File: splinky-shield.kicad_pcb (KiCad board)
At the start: 2 copper layers, 73.5 x 50.8 mm, 55 parts, among them J1 USB_C_Receptacle_USB2.0, J10 Ribbon, J2 Conn_01x04_Female, J3 Conn_01x04_Female, J5 Conn_01x02, J50 Conn_01x04_Female, J6 Serial, J7 trackball, J8 Ribbon, J9 RGB, SW1 SW_Push, SW2 SW_Push, SW3 SW_SPST, U1 RP2040, U2 GD25Q80CEIGR, U3 XC6210B332MR-G, Y1 Crystal_GND24

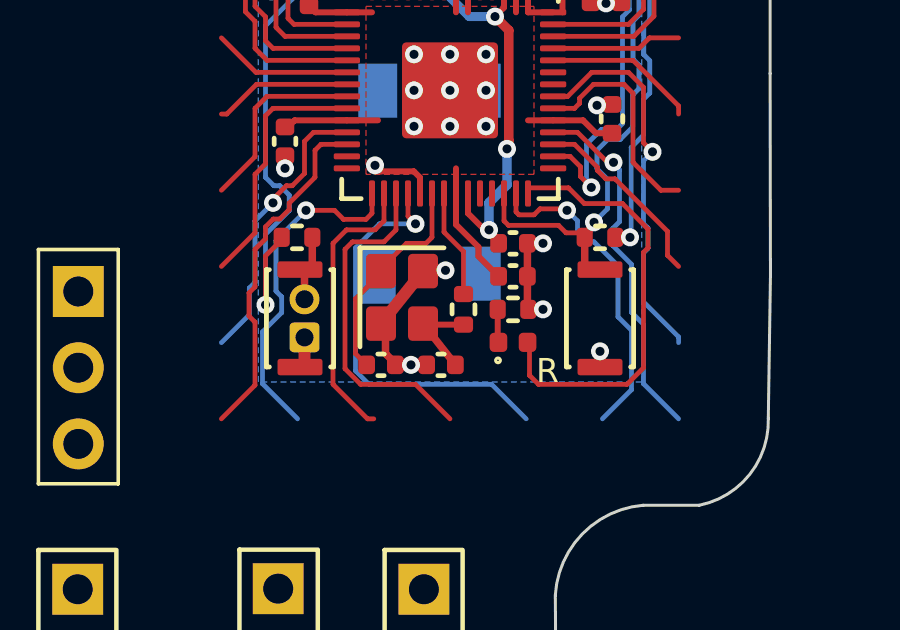
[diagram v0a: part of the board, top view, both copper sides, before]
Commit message: remove buttons
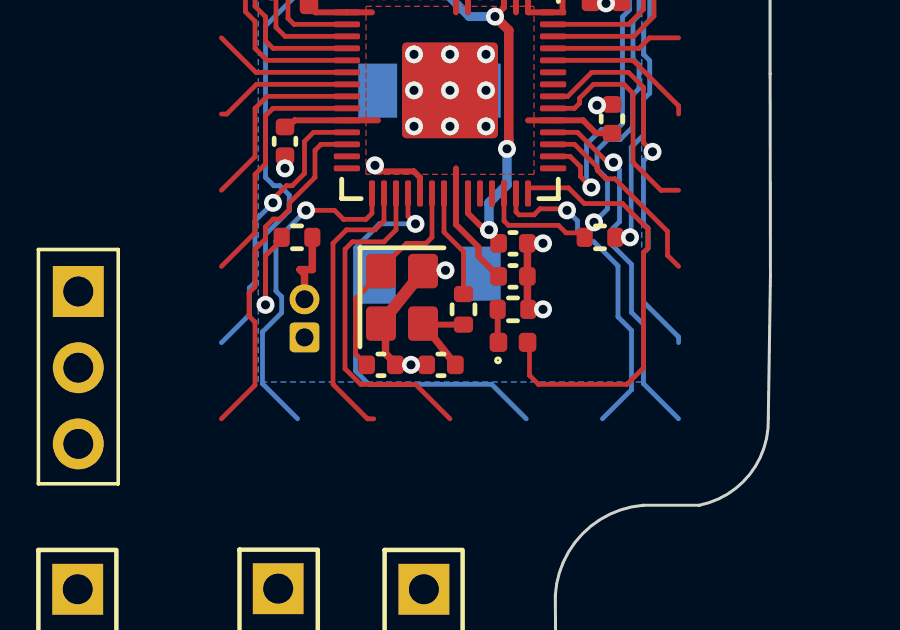
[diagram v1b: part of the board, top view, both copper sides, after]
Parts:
- removed SW1, SW2: SW_Push, Button_Switch_SMD:SW_SPST_CK_KXT3
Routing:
- net GND: track 24.8 -> 23.2 mm, vias 24 -> 23
- net Rst: track 22.0 -> 20.4 mm
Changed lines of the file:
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@@
     )
   )
-  (footprint "Button_Switch_SMD:SW_SPST_CK_KXT3" (layer "F.Cu")
-    (at 147.4 104.6 90)
-    (descr "https://www.ckswitches.com/media/1465/kxt3.pdf")
-    (tags "Switch SPST KXT3")
-    (property "LCSC" "C319433")
-    (property "Sheetfile" "splinky-shield.kicad_sch")
-    (property "Sheetname" "")
-    (attr smd)
-    (fp_text reference "SW2" (at 0 -2 90) (layer "F.SilkS") hide
-      (effects (font (size 1 1) (thickness 0.15)))
-    )
-    (fp_text value "SW_Push" (at 0 2 90) (layer "F.Fab")
-      (effects (font (size 1 1) (thickness 0.15)))
-    )
-    (fp_text user "${REFERENCE}" (at 0 0 90) (layer "F.Fab") hide
-      (effects (font (size 0.5 0.5) (thickness 0.075)))
-    )
-    (fp_line (start 1.62 -1.12) (end 1.62 -1.02) (layer "F.SilkS") (width 0.16))
-    (fp_line (start 1.62 1.02) (end 1.62 1.12) (layer "F.SilkS") (width 0.16))
-    (fp_line (start -1.62 1.12) (end 1.62 1.12) (layer "F.SilkS") (width 0.16))
-    (fp_line (start -1.62 1.02) (end -1.62 1.12) (layer "F.SilkS") (width 0.16))
-    (fp_line (start -1.62 -1.12) (end 1.62 -1.12) (layer "F.SilkS") (width 0.16))
-    (fp_line (start -1.62 -1.12) (end -1.62 -1.02) (layer "F.SilkS") (width 0.16))
-    (fp_line (start 2.15 -1.25) (end 2.15 1.25) (layer "F.CrtYd") (width 0.05))
-    (fp_line (start -2.15 1.25) (end 2.15 1.25) (layer "F.CrtYd") (width 0.05))
-    (fp_line (start -2.15 -1.25) (end 2.15 -1.25) (layer "F.CrtYd") (width 0.05))
-    (fp_line (start -2.15 -1.25) (end -2.15 1.25) (layer "F.CrtYd") (width 0.05))
-    (fp_line (start -1.75 0.65) (end -1.5 0.65) (layer "F.Fab") (width 0.1))
-    (fp_line (start -1.5 -1) (end 1.5 -1) (layer "F.Fab") (width 0.1))
-    (fp_line (start 1.75 0.4) (end 1.75 0.65) (layer "F.Fab") (width 0.1))
-    (fp_line (start 1.75 -0.65) (end 1.75 -0.4) (layer "F.Fab") (width 0.1))
-    (fp_line (start -1.75 -0.65) (end -1.75 -0.4) (layer "F.Fab") (width 0.1))
-    (fp_line (start -1.75 0.4) (end -1.75 0.65) (layer "F.Fab") (width 0.1))
-    (fp_line (start -1.75 -0.4) (end -1.5 -0.15) (layer "F.Fab") (width 0.1))
-    (fp_line (start 1.75 -0.4) (end 1.5 -0.15) (layer "F.Fab") (width 0.1))
-    (fp_line (start 1.5 -0.65) (end 1.75 -0.65) (layer "F.Fab") (width 0.1))
-    (fp_line (start -1.5 0.15) (end -1.75 0.4) (layer "F.Fab") (width 0.1))
-    (fp_line (start 1.5 0.15) (end 1.75 0.4) (layer "F.Fab") (width 0.1))
-    (fp_line (start -1.5 -0.65) (end -1.75 -0.65) (layer "F.Fab") (width 0.1))
-    (fp_line (start 1.75 0.65) (end 1.5 0.65) (layer "F.Fab") (width 0.1))
-    (fp_line (start 1.5 1) (end -1.5 1) (layer "F.Fab") (width 0.1))
-    (fp_line (start -1.5 1) (end -1.5 -1) (layer "F.Fab") (width 0.1))
-    (fp_line (start 1.5 -1) (end 1.5 1) (layer "F.Fab") (width 0.1))
-    (pad "1" smd roundrect (at -1.625 0 90) (size 0.55 1.5) (layers "F.Cu" "F.Paste" "F.Mask") (roundrect_rratio 0.15)
-      (net 2 "GND") (pinfunction "1") (pintype "passive"))
-    (pad "2" smd roundrect (at 1.625 0 90) (size 0.55 1.5) (layers "F.Cu" "F.Paste" "F.Mask") (roundrect_rratio 0.15)
-      (net 47 "Net-(J5-Pad2)") (pinfunction "2") (pintype "passive"))
-    (model "${KICAD6_3DMODEL_DIR}/Button_Switch_SMD.3dshapes/SW_SPST_CK_KXT3.wrl"
-      (offset (xyz 0 0 0))
-      (scale (xyz 1 1 1))
-      (rotate (xyz 0 0 0))
-    )
-    (model "${KICAD6_USER_LIB}/3D_models/SW_SPST_CnK_KXT3.step"
-      (offset (xyz 0 0 0))
-      (scale (xyz 1 1 1))
-      (rotate (xyz 0 0 0))
-    )
-  )
   (footprint "Capacitor_SMD:C_0402_1005Metric" (layer "F.Cu")
     (at 154.5 102.1)
@@
     )
   )
-  (footprint "Button_Switch_SMD:SW_SPST_CK_KXT3" (layer "F.Cu")
-    (at 157.4 104.6 90)
-    (descr "https://www.ckswitches.com/media/1465/kxt3.pdf")
-    (tags "Switch SPST KXT3")
-    (property "LCSC" "C319433")
-    (property "Sheetfile" "splinky-shield.kicad_sch")
-    (property "Sheetname" "")
-    (attr smd)
-    (fp_text reference "SW1" (at 0 -2 90) (layer "F.SilkS") hide
-      (effects (font (size 1 1) (thickness 0.15)))
-    )
-    (fp_text value "SW_Push" (at 0 2 90) (layer "F.Fab")
-      (effects (font (size 1 1) (thickness 0.15)))
-    )
-    (fp_text user "R" (at -1.75 -1.75 unlocked) (layer "F.SilkS")
-      (effects (font (size 0.8 0.8) (thickness 0.2)))
-    )
-    (fp_text user "${REFERENCE}" (at 0 0 90) (layer "F.Fab") hide
-      (effects (font (size 0.5 0.5) (thickness 0.075)))
-    )
-    (fp_line (start -1.62 1.12) (end 1.62 1.12) (layer "F.SilkS") (width 0.16))
-    (fp_line (start -1.62 -1.12) (end 1.62 -1.12) (layer "F.SilkS") (width 0.16))
-    (fp_line (start 1.62 -1.12) (end 1.62 -1.02) (layer "F.SilkS") (width 0.16))
-    (fp_line (start 1.62 1.02) (end 1.62 1.12) (layer "F.SilkS") (width 0.16))
-    (fp_line (start -1.62 1.02) (end -1.62 1.12) (layer "F.SilkS") (width 0.16))
-    (fp_line (start -1.62 -1.12) (end -1.62 -1.02) (layer "F.SilkS") (width 0.16))
-    (fp_line (start -2.15 -1.25) (end 2.15 -1.25) (layer "F.CrtYd") (width 0.05))
-    (fp_line (start 2.15 -1.25) (end 2.15 1.25) (layer "F.CrtYd") (width 0.05))
-    (fp_line (start -2.15 1.25) (end 2.15 1.25) (layer "F.CrtYd") (width 0.05))
-    (fp_line (start -2.15 -1.25) (end -2.15 1.25) (layer "F.CrtYd") (width 0.05))
-    (fp_line (start -1.75 -0.4) (end -1.5 -0.15) (layer "F.Fab") (width 0.1))
-    (fp_line (start -1.5 -1) (end 1.5 -1) (layer "F.Fab") (width 0.1))
-    (fp_line (start -1.75 0.4) (end -1.75 0.65) (layer "F.Fab") (width 0.1))
-    (fp_line (start 1.75 -0.4) (end 1.5 -0.15) (layer "F.Fab") (width 0.1))
-    (fp_line (start 1.5 -0.65) (end 1.75 -0.65) (layer "F.Fab") (width 0.1))
-    (fp_line (start 1.5 0.15) (end 1.75 0.4) (layer "F.Fab") (width 0.1))
-    (fp_line (start -1.5 -0.65) (end -1.75 -0.65) (layer "F.Fab") (width 0.1))
-    (fp_line (start 1.75 -0.65) (end 1.75 -0.4) (layer "F.Fab") (width 0.1))
-    (fp_line (start -1.5 0.15) (end -1.75 0.4) (layer "F.Fab") (width 0.1))
-    (fp_line (start -1.5 1) (end -1.5 -1) (layer "F.Fab") (width 0.1))
-    (fp_line (start 1.75 0.4) (end 1.75 0.65) (layer "F.Fab") (width 0.1))
-    (fp_line (start 1.5 -1) (end 1.5 1) (layer "F.Fab") (width 0.1))
-    (fp_line (start 1.5 1) (end -1.5 1) (layer "F.Fab") (width 0.1))
-    (fp_line (start 1.75 0.65) (end 1.5 0.65) (layer "F.Fab") (width 0.1))
-    (fp_line (start -1.75 0.65) (end -1.5 0.65) (layer "F.Fab") (width 0.1))
-    (fp_line (start -1.75 -0.65) (end -1.75 -0.4) (layer "F.Fab") (width 0.1))
-    (pad "1" smd roundrect (at -1.625 0 90) (size 0.55 1.5) (layers "F.Cu" "F.Paste" "F.Mask") (roundrect_rratio 0.15)
-      (net 2 "GND") (pinfunction "1") (pintype "passive"))
-    (pad "2" smd roundrect (at 1.625 0 90) (size 0.55 1.5) (layers "F.Cu" "F.Paste" "F.Mask") (roundrect_rratio 0.15)
-      (net 38 "Rst") (pinfunction "2") (pintype "passive"))
-    (model "${KICAD6_3DMODEL_DIR}/Button_Switch_SMD.3dshapes/SW_SPST_CK_KXT3.wrl"
-      (offset (xyz 0 0 0))
-      (scale (xyz 1 1 1))
-      (rotate (xyz 0 0 0))
-    )
-    (model "${KICAD6_USER_LIB}/3D_models/SW_SPST_CnK_KXT3.step"
-      (offset (xyz 0 0 0))
-      (scale (xyz 1 1 1))
-      (rotate (xyz 0 0 0))
-    )
-  )
   (footprint "Library:Jack_3.5mm_PJ320E_Horizontal" (layer "F.Cu")
     (at 133.871977 86.43064)
@@
   (segment (start 155.5 104.3) (end 155.01 104.3) (width 0.25) (layer "F.Cu") (net 2))
   (segment (start 154.9 87.2) (end 154.65 86.95) (width 0.4) (layer "F.Cu") (net 2))
-  (segment (start 147.55 106.075) (end 147.4 106.225) (width 0.4) (layer "F.Cu") (net 2))
   (segment (start 157.6 92.12) (end 157.08 92.12) (width 0.16) (layer "F.Cu") (net 2))
   (segment (start 151.5 103.025) (end 150.1 104.775) (width 0.4) (layer "F.Cu") (net 2))
@@
   (segment (start 151.1 106.15) (end 151.62 106.15) (width 0.4) (layer "F.Cu") (net 2))
   (segment (start 150.58 106.105) (end 150.25 105.775) (width 0.25) (layer "F.Cu") (net 2))
-  (segment (start 157.4 105.7) (end 157.4 106.225) (width 0.4) (layer "F.Cu") (net 2))
   (segment (start 157.62 94.08) (end 157.6 94.1) (width 0.25) (layer "F.Cu") (net 2))
   (segment (start 154.98 103.2) (end 154.98 104.27) (width 0.25) (layer "F.Cu") (net 2))
@@
   (segment (start 157.58 94.08) (end 157.6 94.1) (width 0.25) (layer "F.Cu") (net 2))
   (segment (start 154.8 89.45) (end 155.5 89.45) (width 0.6) (layer "F.Cu") (net 2))
-  (segment (start 147.55 105.235) (end 147.55 106.075) (width 0.4) (layer "F.Cu") (net 2))
   (segment (start 151.4 99.905705) (end 151.4 100.4375) (width 0.2) (layer "F.Cu") (net 2))
   (segment (start 150.10048 99.70048) (end 151.194775 99.70048) (width 0.2) (layer "F.Cu") (net 2))
@@
   (via (at 153.6 97) (size 0.6) (drill 0.3) (layers "F.Cu" "B.Cu") (net 2))
   (via (at 152.4 97) (size 0.6) (drill 0.3) (layers "F.Cu" "B.Cu") (net 2))
-  (via (at 157.4 105.7) (size 0.6) (drill 0.3) (layers "F.Cu" "B.Cu") (net 2))
   (via (at 146.9 99.6) (size 0.6) (drill 0.3) (layers "F.Cu" "B.Cu") (free) (net 2))
   (via (at 151.5 90.95) (size 0.6) (drill 0.3) (layers "F.Cu" "B.Cu") (free) (net 2))
@@
   (segment (start 158.05 99.65) (end 158.05 101.380447) (width 0.16) (layer "B.Cu") (net 36))
   (segment (start 156.9 101.91) (end 156.74 101.75) (width 0.16) (layer "F.Cu") (net 38))
-  (segment (start 157.4 102.975) (end 156.925 102.975) (width 0.25) (layer "F.Cu") (net 38))
   (segment (start 154.35 101.5) (end 154.2 101.35) (width 0.16) (layer "F.Cu") (net 38))
   (segment (start 157.2 101.4) (end 156.89 101.9) (width 0.25) (layer "F.Cu") (net 38))
@@
   (segment (start 154.2 101.35) (end 154.2 100.4375) (width 0.16) (layer "F.Cu") (net 38))
   (segment (start 157.2 101.4) (end 156.9 101.91) (width 0.16) (layer "F.Cu") (net 38))
-  (segment (start 156.925 102.975) (end 156.89 102.94) (width 0.25) (layer "F.Cu") (net 38))
-  (segment (start 156.89 102.94) (end 156.89 101.9) (width 0.25) (layer "F.Cu") (net 38))
   (segment (start 156.74 101.75) (end 156.269553 101.75) (width 0.16) (layer "F.Cu") (net 38))
   (segment (start 156.019553 101.5) (end 154.35 101.5) (width 0.16) (layer "F.Cu") (net 38))

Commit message: rst button both sides...
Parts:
- added SW3: SW_SPST, Library:PushSwitch, F.Cu at (151.8, 100.1)
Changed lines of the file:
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@@
+    )
+  )
+  (footprint "Library:PushSwitch" (layer "F.Cu")
+    (at 151.79 100.09 -90)
+    (descr "tactile push button, 6x6mm e.g. PTS645xx series, height=9.5mm")
+    (tags "tact sw push 6mm smd")
+    (property "Sheetfile" "splinky-shield.kicad_sch")
+    (property "Sheetname" "")
+    (attr smd exclude_from_pos_files)
+    (fp_text reference "SW3" (at 0 -4 90) (layer "F.SilkS") hide
+      (effects (font (size 1 1) (thickness 0.15)))
+    )
+    (fp_text value "SW_SPST" (at 0 4.15 90) (layer "F.Fab")
+      (effects (font (size 1 1) (thickness 0.15)))
+    )
+    (fp_text user "${REFERENCE}" (at 0 -4 90) (layer "F.Fab")
+      (effects (font (size 1 1) (thickness 0.15)))
+    )
+    (fp_line (start -3 3) (end 3 3) (layer "F.Fab") (width 0.1))
+    (fp_line (start 3 -3) (end -3 -3) (layer "F.Fab") (width 0.1))
+    (fp_line (start 3 3) (end 3 -3) (layer "F.Fab") (width 0.1))
+    (fp_line (start -3 -3) (end -3 3) (layer "F.Fab") (width 0.1))
+    (fp_circle (center 0 0) (end 1 0) (layer "F.Fab") (width 0.1) (fill none))
+    (pad "1" smd rect (at 3.1 -1.8 270) (size 1.8 1.3) (layers "F.Cu" "F.Paste" "F.Mask")
+      (pinfunction "A") (pintype "passive"))
+    (pad "1" smd rect (at -3.1 -1.75 270) (size 1.8 1.3) (layers "F.Cu" "F.Paste" "F.Mask")
+      (pinfunction "A") (pintype "passive"))
+    (pad "2" smd rect (at -3.1 1.7 270) (size 1.8 1.3) (layers "F.Cu" "F.Paste" "F.Mask")
+      (pinfunction "B") (pintype "passive"))
+    (pad "2" smd rect (at 3 1.7 270) (size 1.8 1.3) (layers "F.Cu" "F.Paste" "F.Mask")
+      (pinfunction "B") (pintype "passive"))
+    (model "${KISYS3DMOD}/Button_Switch_SMD.3dshapes/SW_PUSH_6mm_H9.5mm.wrl"
+      (offset (xyz 0 0 0))
+      (scale (xyz 1 1 1))
+      (rotate (xyz 0 0 0))
     )
   )

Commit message: rst button :(
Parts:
- renumbered SW3 to SW1
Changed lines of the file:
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@@
     )
   )
-  (footprint "Library:PushSwitch" (layer "F.Cu")
+  (footprint "Library:PushSwitch" locked (layer "F.Cu")
     (at 151.79 100.09 -90)
     (descr "tactile push button, 6x6mm e.g. PTS645xx series, height=9.5mm")
@@
     (property "Sheetname" "")
     (attr smd exclude_from_pos_files)
-    (fp_text reference "SW3" (at 0 -4 90) (layer "F.SilkS") hide
+    (fp_text reference "SW1" (at 0 -4 90) (layer "F.SilkS") hide
       (effects (font (size 1 1) (thickness 0.15)))
     )
@@
     (fp_line (start -3 -3) (end -3 3) (layer "F.Fab") (width 0.1))
     (fp_circle (center 0 0) (end 1 0) (layer "F.Fab") (width 0.1) (fill none))
-    (pad "1" smd rect (at 3.1 -1.8 270) (size 1.8 1.3) (layers "F.Cu" "F.Paste" "F.Mask")
+    (pad "1" smd rect locked (at 3.1 -1.8 270) (size 1.8 1.3) (layers "F.Cu" "F.Paste" "F.Mask")
       (pinfunction "A") (pintype "passive"))
-    (pad "1" smd rect (at -3.1 -1.75 270) (size 1.8 1.3) (layers "F.Cu" "F.Paste" "F.Mask")
+    (pad "1" smd rect locked (at -3.1 -1.75 270) (size 1.8 1.3) (layers "F.Cu" "F.Paste" "F.Mask")
       (pinfunction "A") (pintype "passive"))
-    (pad "2" smd rect (at -3.1 1.7 270) (size 1.8 1.3) (layers "F.Cu" "F.Paste" "F.Mask")
+    (pad "2" smd rect locked (at -3.1 1.7 270) (size 1.8 1.3) (layers "F.Cu" "F.Paste" "F.Mask")
       (pinfunction "B") (pintype "passive"))
-    (pad "2" smd rect (at 3 1.7 270) (size 1.8 1.3) (layers "F.Cu" "F.Paste" "F.Mask")
+    (pad "2" smd rect locked (at 3 1.7 270) (size 1.8 1.3) (layers "F.Cu" "F.Paste" "F.Mask")
       (pinfunction "B") (pintype "passive"))
     (model "${KISYS3DMOD}/Button_Switch_SMD.3dshapes/SW_PUSH_6mm_H9.5mm.wrl"
@@
       ) (layer "B.SilkS") (width 0) (fill solid))
   )
-  (footprint "Library:PushSwitch" (layer "B.Cu")
+  (footprint "Library:PushSwitch" locked (layer "B.Cu")
     (at 151.74 100.11 -90)
     (descr "tactile push button, 6x6mm e.g. PTS645xx series, height=9.5mm")
@@
     (fp_line (start -3 3) (end -3 -3) (layer "B.Fab") (width 0.1))
     (fp_circle (center 0 0) (end 1 0) (layer "B.Fab") (width 0.1) (fill none))
-    (pad "1" smd rect (at 3.1 1.8 270) (size 1.8 1.3) (layers "B.Cu" "B.Paste" "B.Mask")
+    (pad "1" smd rect locked (at 3.1 1.8 270) (size 1.8 1.3) (layers "B.Cu" "B.Paste" "B.Mask")
       (net 38 "Rst") (pinfunction "A") (pintype "passive"))
-    (pad "1" smd rect (at -3.1 1.75 270) (size 1.8 1.3) (layers "B.Cu" "B.Paste" "B.Mask")
+    (pad "1" smd rect locked (at -3.1 1.75 270) (size 1.8 1.3) (layers "B.Cu" "B.Paste" "B.Mask")
       (net 38 "Rst") (pinfunction "A") (pintype "passive"))
-    (pad "2" smd rect (at -3.1 -1.7 270) (size 1.8 1.3) (layers "B.Cu" "B.Paste" "B.Mask")
+    (pad "2" smd rect locked (at -3.1 -1.7 270) (size 1.8 1.3) (layers "B.Cu" "B.Paste" "B.Mask")
       (net 2 "GND") (pinfunction "B") (pintype "passive"))
-    (pad "2" smd rect (at 3 -1.7 270) (size 1.8 1.3) (layers "B.Cu" "B.Paste" "B.Mask")
+    (pad "2" smd rect locked (at 3 -1.7 270) (size 1.8 1.3) (layers "B.Cu" "B.Paste" "B.Mask")
       (net 2 "GND") (pinfunction "B") (pintype "passive"))
     (model "${KISYS3DMOD}/Button_Switch_SMD.3dshapes/SW_PUSH_6mm_H9.5mm.wrl"

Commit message: routing
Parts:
- removed the J2 at (160.0, 80.0)
- removed J50: Conn_01x04_Female, Library:Jack_3.5mm_PJ320E_Horizontal
- added J11: Serial, drawings:Jack_3.5mm_PJ320E_Horizontal_custom, F.Cu at (133.9, 86.3)
- added J12: Conn_01x04_Female, Connector_PinSocket_2.54mm:PinSocket_1x04_P2.54mm_Vertical, F.Cu at (160.0, 80.0)
- added U4: USBLC6-2P6, Package_TO_SOT_SMD:SOT-666, F.Cu at (192.2, 93.0)
- added kibuzzard-61F01B61: G***, kibuzzard-61F01B61, F.Cu at (137.8, 95.2)
- added kibuzzard-6208EFFE: G***, kibuzzard-6208EFFE, B.Cu at (137.3, 95.2)
- ?: moved to B.Cu
- J6: footprint Library:Jack_3.5mm_PJ320E_Horizontal -> drawings:Jack_3.5mm_PJ320E_Horizontal_custom
- moved R4 75.6 mm to (194.4, 92.5)
- moved R5 69.1 mm to (189.9, 92.5)
- moved FB1 66.4 mm to (187.4, 91.9)
- moved SW1 16.0 mm to (136.1, 97.1)
- moved SW3 16.0 mm to (136.0, 97.0), turned to 90 degrees
- moved D2 5.22 mm to (151.5, 81.6)
- moved F1 5.18 mm to (149.6, 81.5)
- moved U3 5.14 mm to (154.6, 81.8)
- moved C1 5.11 mm to (153.2, 84.3)
- moved C2 5.11 mm to (156.3, 84.3)
- moved JP1 2.95 mm to (140.1, 91.7), turned to -90 degrees
- moved JP2 2.95 mm to (140.1, 91.7), turned to -90 degrees
- moved J6 0.81 mm to (138.5, 86.3)
- turned ? to 180 degrees
- renumbered J3 to J4
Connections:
- FB1 pad 1: GND -> /Gnd_daughter
- J1 pad A1: GND -> /Gnd_daughter
- J1 pad A12: GND -> /Gnd_daughter
- J1 pad A4: VBUS -> /Vbus_daughter
- J1 pad A6: /D+ -> /D+_daughter
- J1 pad A7: /D- -> /D-_daughter
- J1 pad A9: VBUS -> /Vbus_daughter
- J1 pad B1: GND -> /Gnd_daughter
- J1 pad B12: GND -> /Gnd_daughter
- J1 pad B4: VBUS -> /Vbus_daughter
- J1 pad B6: /D+ -> /D+_daughter
- J1 pad B7: /D- -> /D-_daughter
- J1 pad B9: VBUS -> /Vbus_daughter
- J2 pad 1: +5V -> /Vbus_daughter
- J2 pad 2: GND -> /Gnd_daughter
- J2 pad 3: /D- -> /D-_daughter
- J2 pad 4: /D+ -> /D+_daughter
- J3 pad 1: +5V -> /Vbus_daughter
- J3 pad 2: GND -> /Gnd_daughter
- J3 pad 3: /D- -> /D-_daughter
- J3 pad 4: /D+ -> /D+_daughter
- J4 pad 1: +5V -> VBUS
- R4 pad 2: GND -> /Gnd_daughter
- R5 pad 2: GND -> /Gnd_daughter
- SW1 pad 1: (no net) -> Rst
- SW1 pad 2: (no net) -> GND
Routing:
- net miso_l: track 6.40 -> 51.6 mm, vias 0 -> 1
- net sc_l: track 7.42 -> 47.5 mm, vias 0 -> 1
- net row2_l: track 5.08 -> 42.0 mm, vias 0 -> 1
- net col1_l: track 4.33 -> 40.8 mm, vias 0 -> 1
- net col2_l: track 5.80 -> 39.6 mm, vias 0 -> 1
- net mosi_l: track 12.9 -> 44.4 mm
- net row1_l: track 7.83 -> 38.7 mm, vias 0 -> 1
- net col5_l: track 8.44 -> 38.3 mm
- net col4_l: track 6.42 -> 36.1 mm
- net col6_l: track 9.51 -> 38.6 mm, vias 1 -> 0
- net row3_l: track 4.59 -> 33.7 mm
- net row5_l: track 11.7 -> 40.4 mm
- net Rst: track 20.4 -> 48.9 mm, vias 1 -> 3
- net /D-_daughter: track 0.00 -> 27.2 mm, vias 0 -> 2
- net /D+_daughter: track 0.00 -> 25.6 mm, vias 0 -> 2
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- added copper zone on B.Cu, net /Gnd_daughter
- added copper zone on F.Cu, net /Gnd_daughter
- added copper zone on F.Cu, net GND
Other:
- outline, holes or cut-outs redrawn
